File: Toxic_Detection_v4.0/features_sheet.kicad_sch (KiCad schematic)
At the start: 3 parts, among them IC1 ESP32-WROOM-32E-N16

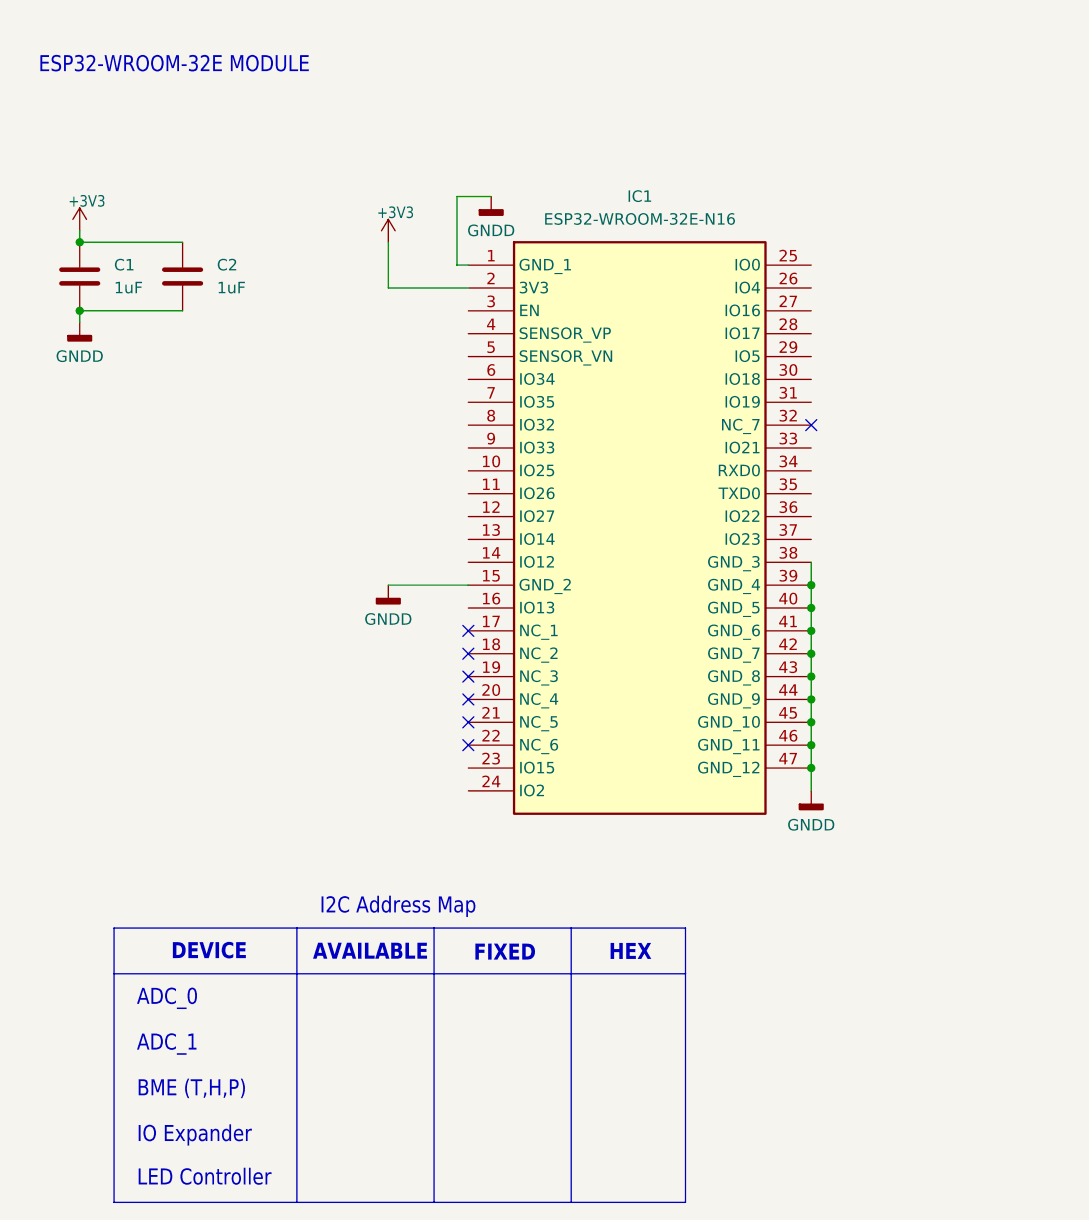
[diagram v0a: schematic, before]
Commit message: feat: add spi between STM32 and ESP32, update JTAG to add ESP32 on it
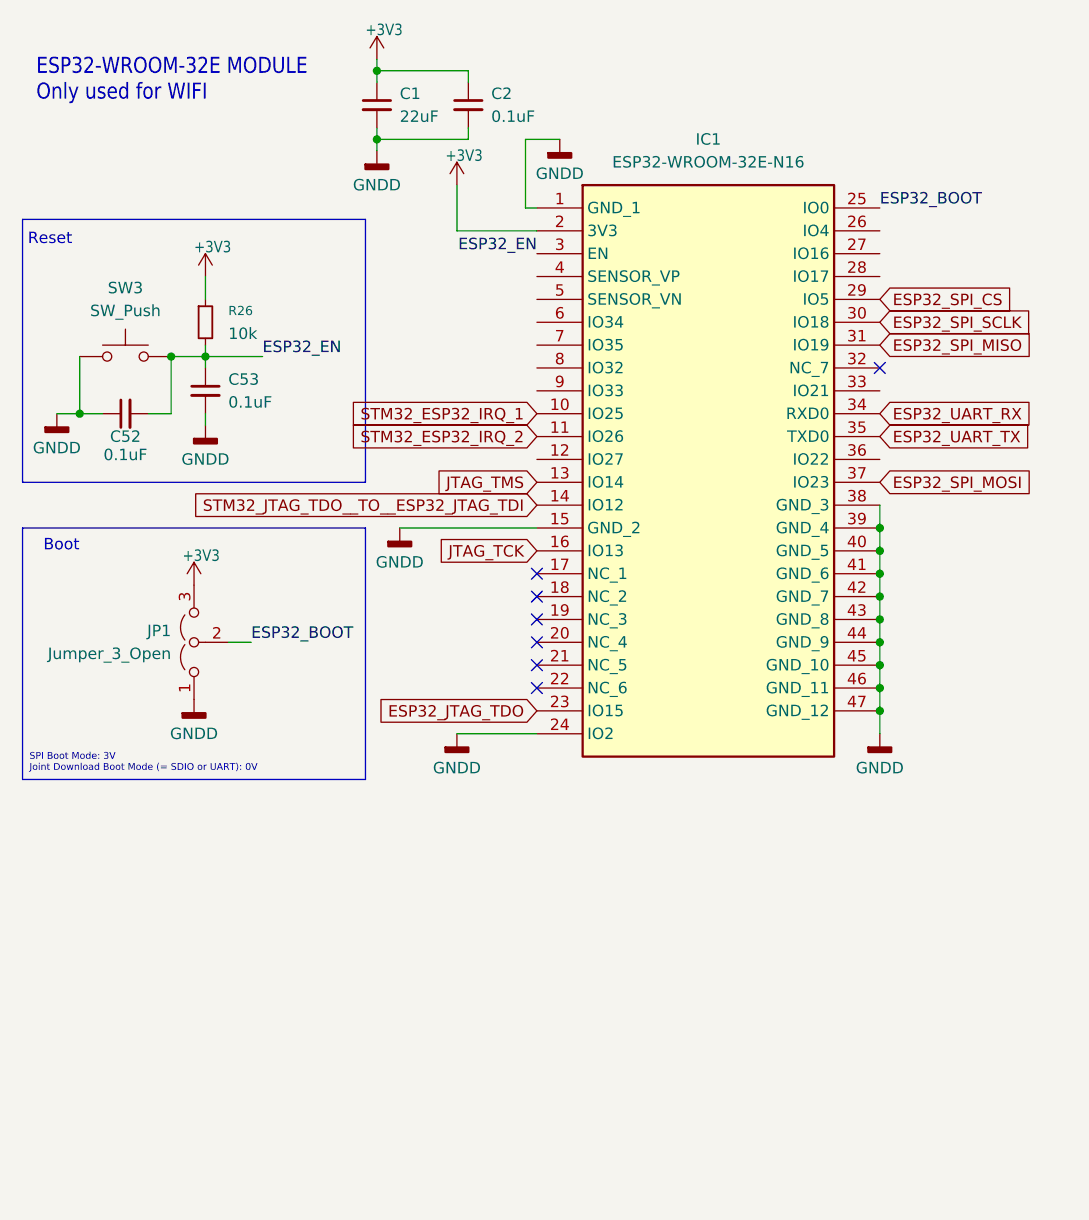
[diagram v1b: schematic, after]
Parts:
- removed C1, C2: 1uF, symbol Device:C
- added C1: 22uF, symbol Device:C_Small
- added C2, C52, C53: 0.1uF, symbol Device:C_Small
- added JP1: Jumper_3_Open, Connector_PinHeader_2.54mm:PinHeader_1x03_P2.54mm_Vertical, symbol Jumper:Jumper_3_Open
- added R26: 10k, symbol Device:R_Small
- added SW3: SW_Push, symbol Switch:SW_Push
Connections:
- net +3V3: now also C1.1, C2.1, JP1.3 (B), R26.1
- net GNDD: now also IC1.24 (IO2), C1.2, C2.2, C52.1, C53.2, JP1.1 (A), SW3.1
- net STM32_ESP32_IRQ_1: now reaches IC1.10 (IO25)
- net STM32_ESP32_IRQ_2: now reaches IC1.11 (IO26)
- net JTAG_TMS: now reaches IC1.13 (IO14)
- net STM32_JTAG_TDO__TO__ESP32_JTAG_TDI: now reaches IC1.14 (IO12)
- net JTAG_TCK: now reaches IC1.16 (IO13)
- net ESP32_JTAG_TDO: now reaches IC1.23 (IO15)
- net ESP32_BOOT: now reaches IC1.25 (IO0)
- net ESP32_BOOT: now also JP1.2 (C)
- net ESP32_SPI_CS: now reaches IC1.29 (IO5)
- net ESP32_EN: now reaches IC1.3 (EN)
- net ESP32_EN: now also C52.2, C53.1, R26.2, SW3.2
- net ESP32_SPI_SCLK: now reaches IC1.30 (IO18)
- net ESP32_SPI_MISO: now reaches IC1.31 (IO19)
- net ESP32_UART_RX: now reaches IC1.34 (RXD0)
- net ESP32_UART_TX: now reaches IC1.35 (TXD0)
- net ESP32_SPI_MOSI: now reaches IC1.37 (IO23)
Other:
- note added: "Boot"
- note added: "ESP32-WROOM-32E MODULE Only used for WIFI"
- note added: "Reset"
- note added: "SPI Boot Mode: 3V Joint Download Boot Mode (= SDIO or UART): 0V"
- note removed: "ADC_0"
- note removed: "ADC_1"
- note removed: "AVAILABLE"
- note removed: "BME (T,H,P)"
- note removed: "DEVICE"
- note removed: "ESP32-WROOM-32E MODULE"
- note removed: "FIXED"
- note removed: "HEX"
- note removed: "I2C Address Map"
- note removed: "IO Expander"
- note removed: "LED Controller"
- moved on the sheet: IC1

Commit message: feat: add GNSS module and antenna
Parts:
- added ANT1: SAM-M10Q-00B, SAMM10Q00B, symbol SAM-M10Q-00B:SAM-M10Q-00B
- added C54: 100nF, symbol Device:C_Small
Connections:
- net +3V3: now also ANT1.17 (VCC), ANT1.2 (V_IO), C54.1
- net GNDD: now also ANT1.1 (GND_1), ANT1.10 (GND_5), ANT1.11 (GND_6), ANT1.15 (GND_7), ANT1.16 (GND_8), ANT1.20 (GND_9), ANT1.4 (GND_2), ANT1.5 (GND_3), ANT1.6 (GND_4), C54.2
- new net SAM_M10Q_EXTINT: ANT1.19 (EXTINT)
- new net SAM_M10Q_NRST: ANT1.18 (RESET_N)
- new net SAM_M10Q_UART_RX: ANT1.14 (RXD)
- new net SAM_M10Q_UART_TX: ANT1.13 (TXD)
- no-connect marks 7 -> 12
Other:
- note added: "GNSS module & antenna"
- moved on the sheet: C1, C2, C52, C53, IC1, JP1, R26, SW3

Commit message: feat: add leds and headers
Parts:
- added J1: Conn_01x11_Pin, symbol Connector:Conn_01x11_Pin
- renumbered C52 to C1, C53 to C2, C1 to C3, C2 to C4, C54 to C5, R26 to R1, SW3 to SW1
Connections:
- net ESP32_IO27: now reaches IC1.12 (IO27)
- net ESP32_IO27: now also J1.5 (Pin_5)
- net ESP32_IO4: now reaches IC1.26 (IO4)
- net ESP32_IO4: now also J1.1 (Pin_1)
- net ESP32_LED_0: now reaches IC1.27 (IO16)
- net ESP32_IO17: now reaches IC1.28 (IO17)
- net ESP32_IO17: now also J1.2 (Pin_2)
- net ESP32_IO21: now reaches IC1.33 (IO21)
- net ESP32_IO21: now also J1.3 (Pin_3)
- net ESP32_IO22: now reaches IC1.36 (IO22)
- net ESP32_IO22: now also J1.4 (Pin_4)
- net ESP32_SEN_VP: now reaches IC1.4 (SENSOR_VP)
- net ESP32_SEN_VP: now also J1.11 (Pin_11)
- net ESP32_SEN_VN: now reaches IC1.5 (SENSOR_VN)
- net ESP32_SEN_VN: now also J1.10 (Pin_10)
- net ESP32_I34: now reaches IC1.6 (IO34)
- net ESP32_I34: now also J1.9 (Pin_9)
- net ESP32_I35: now reaches IC1.7 (IO35)
- net ESP32_I35: now also J1.8 (Pin_8)
- net ESP32_IO32: now reaches IC1.8 (IO32)
- net ESP32_IO32: now also J1.7 (Pin_7)
- net ESP32_IO33: now reaches IC1.9 (IO33)
- net ESP32_IO33: now also J1.6 (Pin_6)
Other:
- note added: "ESP Header"

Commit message: feat: assign footprints and pass ERC
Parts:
- removed C1: 0.1uF, symbol Device:C_Small
- ANT1: footprint SAMM10Q00B -> GNSS module and antenna:SAMM10Q00B
- C1: renamed from C2; value 0.1uF -> 100nF; footprint (none) -> Capacitor_SMD:C_0805_2012Metric_Pad1.18x1.45mm_HandSolder
- C2: renamed from C3; footprint (none) -> Capacitor_SMD:C_0805_2012Metric_Pad1.18x1.45mm_HandSolder
- C3: renamed from C4; value 0.1uF -> 100nF; footprint (none) -> Capacitor_SMD:C_0805_2012Metric_Pad1.18x1.45mm_HandSolder
- C4: renamed from C5; footprint (none) -> Capacitor_SMD:C_0805_2012Metric_Pad1.18x1.45mm_HandSolder
- IC1: footprint ESP32WROOM32EN16 -> ESP32-WROOM-32E-N16:ESP32WROOM32EN16
- J1: footprint (none) -> Connector_PinSocket_2.54mm:PinSocket_1x11_P2.54mm_Vertical
- R1: footprint (none) -> Resistor_SMD:R_0805_2012Metric_Pad1.20x1.40mm_HandSolder
- SW1: footprint (none) -> Button_Switch_THT:SW_PUSH_6mm
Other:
- moved on the sheet: C1

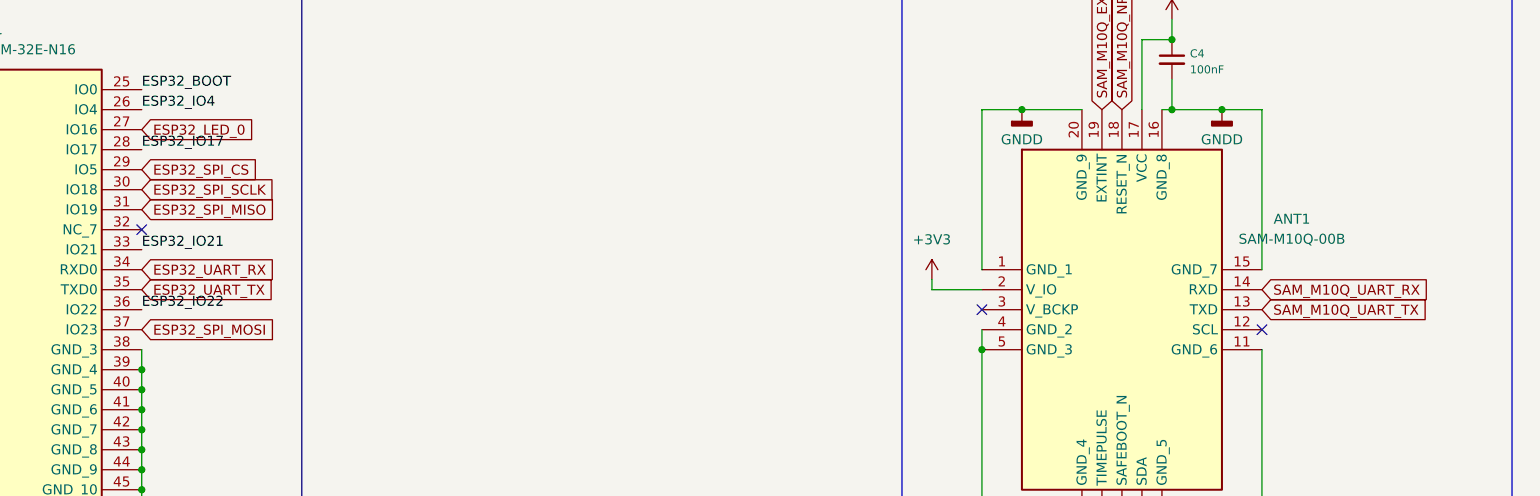
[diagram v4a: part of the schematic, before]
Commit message: doc: update schematic documentation, design notes and all other kind of documentation. Add product_brief revision history
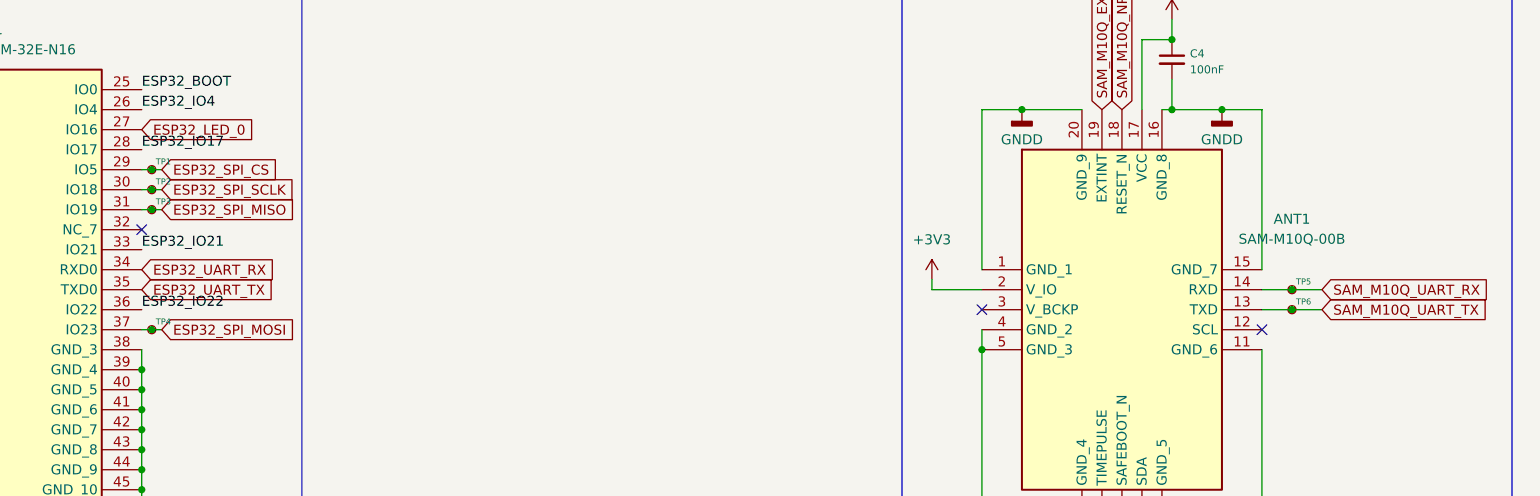
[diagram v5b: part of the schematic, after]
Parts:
- added TP1, TP2, TP3, TP4, TP5, TP6: TestPoint_Small, TestPoint:TestPoint_Pad_D1.0mm, symbol Connector:TestPoint_Small
- JP1: footprint Connector_PinHeader_2.54mm:PinHeader_1x03_P2.54mm_Vertical -> Connector_PinSocket_2.54mm:PinSocket_1x03_P2.54mm_Vertical
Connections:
- net ESP32_SPI_CS: now also TP1.1
- net ESP32_SPI_MISO: now also TP3.1
- net ESP32_SPI_MOSI: now also TP4.1
- net ESP32_SPI_SCLK: now also TP2.1
- net SAM_M10Q_UART_RX: now also TP5.1
- net SAM_M10Q_UART_TX: now also TP6.1
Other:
- company: (none) -> Company: LNIS
- title: (none) -> Toxic_Detection_PCB

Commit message: feat: first placement (layout)
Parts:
- J1: footprint Connector_PinSocket_2.54mm:PinSocket_1x11_P2.54mm_Vertical -> Connector_PinHeader_2.54mm:PinHeader_1x11_P2.54mm_Vertical
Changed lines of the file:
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@@
 		(title "Toxic_Detection_PCB")
 		(date "2026-02-12")
-		(rev "4.0")
+		(rev "4.1")
 		(company "Company: LNIS")
 		(comment 4 "Author: Paul Capgras")
@@
 			)
 		)
-		(property "Footprint" "Connector_PinSocket_2.54mm:PinSocket_1x11_P2.54mm_Vertical"
+		(property "Footprint" "Connector_PinHeader_2.54mm:PinHeader_1x11_P2.54mm_Vertical"
 			(at 36.83 120.65 0)
 			(effects
